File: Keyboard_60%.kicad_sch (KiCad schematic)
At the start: 51 parts, among them J3 Prog_conn, J5 Tag connect TC2030-CTX, SW2 Reset Switch, U3 nRF52840-QIAA-R/nRF52833-QIAA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, Y1 32MHz, Y2 32.768kHz

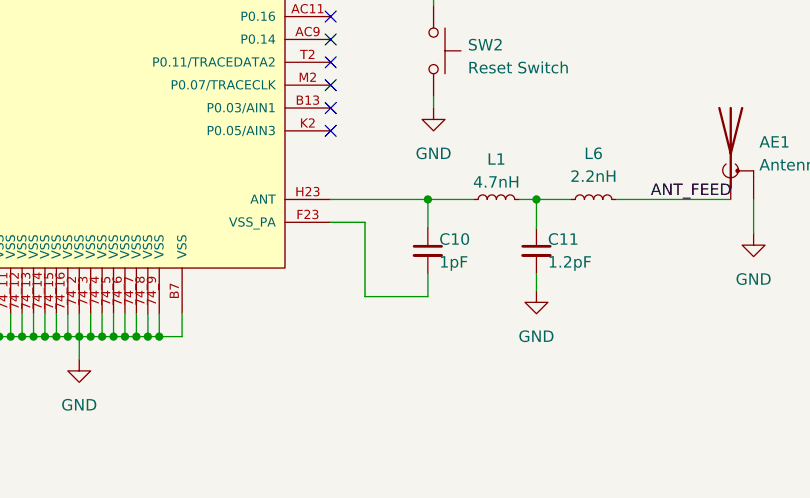
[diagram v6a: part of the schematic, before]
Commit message: Changed the gerber to final production files
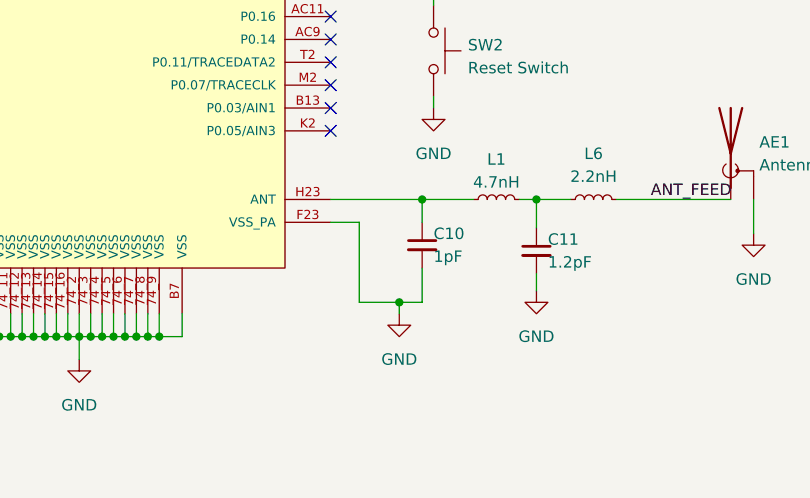
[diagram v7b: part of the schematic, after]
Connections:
- net GND: now also C10.2, U3.F23 (VSS_PA)
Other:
- moved on the sheet: C10
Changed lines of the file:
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@@
   (junction (at 91.44 181.61) (diameter 0) (color 0 0 0 0)
   )
-  (junction (at 130.175 166.37) (diameter 0) (color 0 0 0 0)
-  )
   (junction (at 39.37 87.63) (diameter 0) (color 0 0 0 0)
   )
@@
   (junction (at 86.36 181.61) (diameter 0) (color 0 0 0 0)
   )
+  (junction (at 129.54 166.37) (diameter 0) (color 0 0 0 0)
+  )
   (junction (at 23.495 153.67) (diameter 0) (color 0 0 0 0)
   )
@@
   )
   (junction (at 43.18 99.06) (diameter 0) (color 0 0 0 0)
+  )
+  (junction (at 127 177.8) (diameter 0) (color 0 0 0 0)
   )
   (junction (at 90.17 181.61) (diameter 0) (color 0 0 0 0)
@@
     (stroke (width 0) (type default))
   )
+  (wire (pts (xy 127 177.8) (xy 127 179.07))
+    (stroke (width 0) (type default))
+  )
   (wire (pts (xy 213.36 81.28) (xy 213.36 87.63))
     (stroke (width 0) (type default))
@@
     (stroke (width 0) (type default))
   )
+  (wire (pts (xy 129.54 166.37) (xy 135.255 166.37))
+    (stroke (width 0) (type default))
+  )
   (wire (pts (xy 130.81 144.78) (xy 130.81 143.51))
     (stroke (width 0) (type default))
@@
     (stroke (width 0) (type default))
   )
-  (wire (pts (xy 130.175 166.37) (xy 130.175 169.545))
+  (wire (pts (xy 129.54 166.37) (xy 129.54 168.91))
     (stroke (width 0) (type default))
   )
@@
     (stroke (width 0) (type default))
   )
-  (wire (pts (xy 123.19 168.91) (xy 123.19 177.165))
+  (wire (pts (xy 122.555 168.91) (xy 122.555 177.8))
     (stroke (width 0) (type default))
   )
@@
     (stroke (width 0) (type default))
   )
-  (wire (pts (xy 119.38 166.37) (xy 130.175 166.37))
+  (wire (pts (xy 119.38 166.37) (xy 129.54 166.37))
     (stroke (width 0) (type default))
   )
@@
     (stroke (width 0) (type default))
   )
-  (wire (pts (xy 123.19 177.165) (xy 130.175 177.165))
+  (wire (pts (xy 122.555 177.8) (xy 127 177.8))
     (stroke (width 0) (type default))
   )
@@
     (stroke (width 0) (type default))
   )
+  (wire (pts (xy 127 177.8) (xy 129.54 177.8))
+    (stroke (width 0) (type default))
+  )
   (wire (pts (xy 100.33 179.07) (xy 100.33 181.61))
     (stroke (width 0) (type default))
@@
     (stroke (width 0) (type default))
   )
-  (wire (pts (xy 119.38 168.91) (xy 123.19 168.91))
+  (wire (pts (xy 119.38 168.91) (xy 122.555 168.91))
     (stroke (width 0) (type default))
   )
@@
     (stroke (width 0) (type default))
   )
-  (wire (pts (xy 135.255 166.37) (xy 130.175 166.37))
-    (stroke (width 0) (type default))
-  )
   (wire (pts (xy 91.44 179.07) (xy 91.44 181.61))
     (stroke (width 0) (type default))
   )
-  (wire (pts (xy 130.175 177.165) (xy 130.175 174.625))
+  (wire (pts (xy 129.54 173.99) (xy 129.54 177.8))
     (stroke (width 0) (type default))
   )
@@
     )
   )
-  (symbol (lib_id "keyboard:C_Small") (at 130.175 172.085 0) (unit 1)
-    (in_bom yes) (on_board yes) (dnp no)
-    (property "Reference" "C10" (at 131.445 170.815 0)
+  (symbol (lib_id "keyboard:C_Small") (at 129.54 171.45 0) (unit 1)
+    (in_bom yes) (on_board yes) (dnp no)
+    (property "Reference" "C10" (at 130.81 170.18 0)
       (effects (font (size 1.27 1.27)) (justify left))
     )
-    (property "Value" "1pF" (at 131.445 173.355 0)
+    (property "Value" "1pF" (at 130.81 172.72 0)
       (effects (font (size 1.27 1.27)) (justify left))
     )
-    (property "Footprint" "keyboard:C_0402_1005Metric" (at 130.175 172.085 0)
-      (effects (font (size 1.27 1.27)) hide)
-    )
-    (property "Datasheet" "https://datasheet.lcsc.com/lcsc/2304140030_YAGEO-CC0402BRNPO9BN1R0_C309455.pdf" (at 130.175 172.085 0)
-      (effects (font (size 1.27 1.27)) hide)
-    )
-    (property "PN" "CC0402BRNPO9BN1R0" (at 130.175 172.085 0)
-      (effects (font (size 1.27 1.27)) hide)
-    )
-    (property "LCSC Part Number" "C309455" (at 130.175 172.085 0)
-      (effects (font (size 1.27 1.27)) hide)
-    )
-    (property "LCSC link" "https://www.lcsc.com/product-detail/Multilayer-Ceramic-Capacitors-MLCC-SMD-SMT_YAGEO-CC0402BRNPO9BN1R0_C309455.html" (at 130.175 172.085 0)
+    (property "Footprint" "keyboard:C_0402_1005Metric" (at 129.54 171.45 0)
+      (effects (font (size 1.27 1.27)) hide)
+    )
+    (property "Datasheet" "https://datasheet.lcsc.com/lcsc/2304140030_YAGEO-CC0402BRNPO9BN1R0_C309455.pdf" (at 129.54 171.45 0)
+      (effects (font (size 1.27 1.27)) hide)
+    )
+    (property "PN" "CC0402BRNPO9BN1R0" (at 129.54 171.45 0)
+      (effects (font (size 1.27 1.27)) hide)
+    )
+    (property "LCSC Part Number" "C309455" (at 129.54 171.45 0)
+      (effects (font (size 1.27 1.27)) hide)
+    )
+    (property "LCSC link" "https://www.lcsc.com/product-detail/Multilayer-Ceramic-Capacitors-MLCC-SMD-SMT_YAGEO-CC0402BRNPO9BN1R0_C309455.html" (at 129.54 171.45 0)
       (effects (font (size 1.27 1.27)) hide)
     )
@@
         )
       )
+    )
+  )
+  (symbol (lib_id "power:GND") (at 127 179.07 0) (unit 1)
+    (in_bom yes) (on_board yes) (dnp no) (fields_autoplaced)
+    (property "Reference" "#PWR07" (at 127 185.42 0)
+      (effects (font (size 1.27 1.27)) hide)
+    )
+    (property "Value" "GND" (at 127 184.15 0)
+      (effects (font (size 1.27 1.27)))
+    )
+    (property "Footprint" "" (at 127 179.07 0)
+      (effects (font (size 1.27 1.27)) hide)
+    )
+    (property "Datasheet" "" (at 127 179.07 0)
+      (effects (font (size 1.27 1.27)) hide)
+    )
+    (pin "1")
+    (instances
+      (project "Keyboard_60%"
+        (path "/ef112b03-6536-453f-8127-17d1495b48aa/01d5aa47-03a0-4747-998b-393b2b88e5ef"
+          (reference "#PWR07") (unit 1)
+        )
+        (path "/ef112b03-6536-453f-8127-17d1495b48aa"
+          (reference "#PWR08") (unit 1)
+        )
+      )
